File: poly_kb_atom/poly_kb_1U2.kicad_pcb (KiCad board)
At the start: 2 copper layers, 19 x 38.1 mm, 38 parts, among them J1 Conn_01x16, J2 North, J3 WestFront, J4 EastFront, J5 WestBack, J6 EastBack, J7 South, J8 North2, J9 South2, SW1 SW_Push

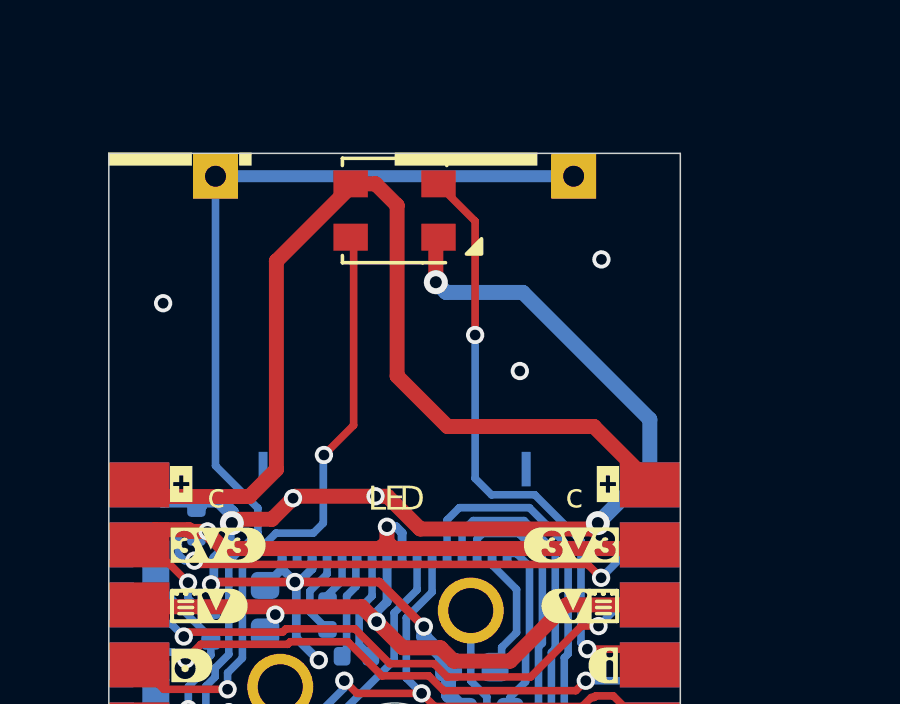
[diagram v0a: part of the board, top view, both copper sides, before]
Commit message: Added optional C7 and fix LED silkscreens
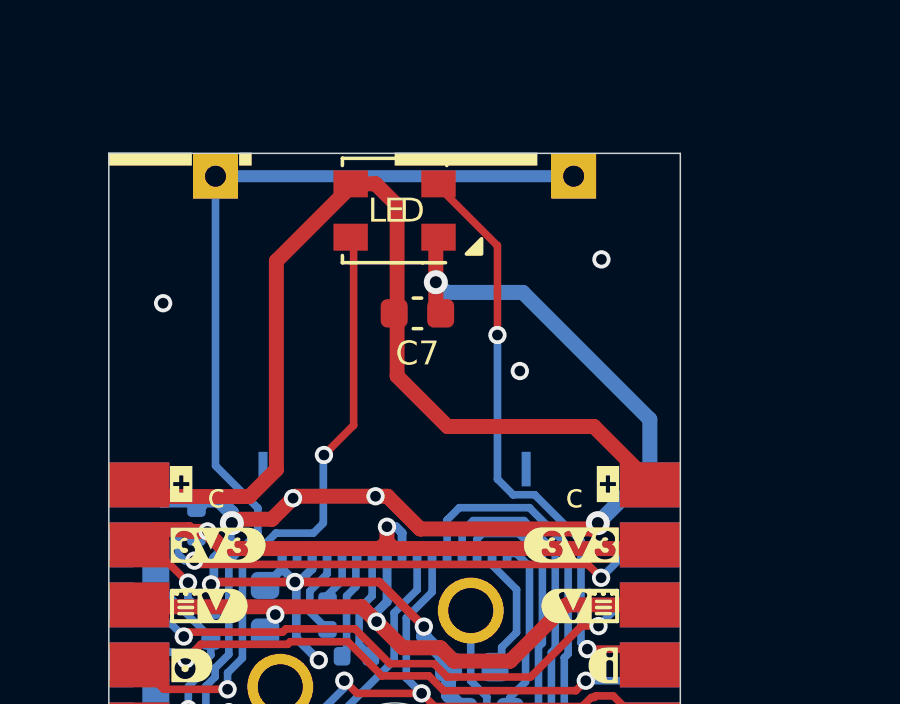
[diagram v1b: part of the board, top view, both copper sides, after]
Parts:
- added C7: 100nF, Capacitor_SMD:C_0603_1608Metric, F.Cu at (102.5, 50.0)
- LED1: value LED -> WS2812B-Mini
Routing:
- net /Keyboard/sheet605ED2EB/GND: track 52.9 -> 54.0 mm
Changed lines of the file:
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@@
       (effects (font (size 0.6 0.6) (thickness 0.15)))
     )
-    (fp_text value "LED" (at 0 0 180) (layer "F.Fab")
+    (fp_text value "WS2812B-Mini" (at 0 0 180) (layer "F.Fab")
       (effects (font (size 0.6 0.6) (thickness 0.15)))
     )
@@
       ) (layer "F.SilkS") (width 0) (fill solid))
   )
+  (footprint "Capacitor_SMD:C_0603_1608Metric" (layer "F.Cu")
+    (at 102.489 49.9618)
+    (descr "Capacitor SMD 0603 (1608 Metric), square (rectangular) end terminal, IPC_7351 nominal, (Body size source: IPC-SM-782 page 76, https://www.pcb-3d.com/wordpress/wp-content/uploads/ipc-sm-782a_amendment_1_and_2.pdf), generated with kicad-footprint-generator")
+    (tags "capacitor")
+    (property "LCSC" "C19666")
+    (property "Sheetfile" "SSD1306_TO_SPI.kicad_sch")
+    (property "Sheetname" "sheet605ED2EB")
+    (attr smd)
+    (fp_text reference "C7" (at 0 1.3335) (layer "F.SilkS")
+      (effects (font (size 0.8 0.8) (thickness 0.15)))
+    )
+    (fp_text value "100nF" (at 0 1.43) (layer "F.Fab")
+      (effects (font (size 1 1) (thickness 0.15)))
+    )
+    (fp_text user "${REFERENCE}" (at 0 0) (layer "F.Fab")
+      (effects (font (size 0.4 0.4) (thickness 0.06)))
+    )
+    (fp_line (start -0.14058 -0.51) (end 0.14058 -0.51) (layer "F.SilkS") (width 0.12))
+    (fp_line (start -0.14058 0.51) (end 0.14058 0.51) (layer "F.SilkS") (width 0.12))
+    (fp_line (start 1.48 -0.73) (end 1.48 0.73) (layer "F.CrtYd") (width 0.05))
+    (fp_line (start 1.48 0.73) (end -1.48 0.73) (layer "F.CrtYd") (width 0.05))
+    (fp_line (start -1.48 0.73) (end -1.48 -0.73) (layer "F.CrtYd") (width 0.05))
+    (fp_line (start -1.48 -0.73) (end 1.48 -0.73) (layer "F.CrtYd") (width 0.05))
+    (fp_line (start 0.8 0.4) (end -0.8 0.4) (layer "F.Fab") (width 0.1))
+    (fp_line (start 0.8 -0.4) (end 0.8 0.4) (layer "F.Fab") (width 0.1))
+    (fp_line (start -0.8 0.4) (end -0.8 -0.4) (layer "F.Fab") (width 0.1))
+    (fp_line (start -0.8 -0.4) (end 0.8 -0.4) (layer "F.Fab") (width 0.1))
+    (pad "1" smd roundrect (at -0.775 0) (size 0.9 0.95) (layers "F.Cu" "F.Paste" "F.Mask") (roundrect_rratio 0.25)
+      (net 15 "/Keyboard/sheet605ED2EB/5V") (pintype "passive"))
+    (pad "2" smd roundrect (at 0.775 0) (size 0.9 0.95) (layers "F.Cu" "F.Paste" "F.Mask") (roundrect_rratio 0.25)
+      (net 1 "/Keyboard/sheet605ED2EB/GND") (pintype "passive"))
+    (model "${KICAD6_3DMODEL_DIR}/Capacitor_SMD.3dshapes/C_0603_1608Metric.wrl"
+      (offset (xyz 0 0 0))
+      (scale (xyz 1 1 1))
+      (rotate (xyz 0 0 0))
+    )
+  )
   (footprint "kibuzzard-61EFBE87" (layer "F.Cu")
     (at 96.0374 59.7154)
@@
     (effects (font (size 0.8 0.8) (thickness 0.153)))
   )
-  (gr_text "E" (at 101.727 56.134) (layer "F.SilkS")
+  (gr_text "E" (at 101.727 46.5328) (layer "F.SilkS")
     (effects (font (size 0.8 0.8) (thickness 0.15)))
   )
-  (gr_text "D" (at 102.3112 56.134) (layer "F.SilkS")
+  (gr_text "D" (at 102.3112 46.5328) (layer "F.SilkS")
     (effects (font (size 0.8 0.8) (thickness 0.15)))
   )
-  (gr_text "L" (at 101.1428 56.134) (layer "F.SilkS")
+  (gr_text "L" (at 101.1428 46.5328) (layer "F.SilkS")
     (effects (font (size 0.8 0.8) (thickness 0.15)))
   )
@@
   (segment (start 101.092 56.0578) (end 98.407521 56.0578) (width 0.5) (layer "F.Cu") (net 1))
   (segment (start 95.662917 58.91646) (end 95.585745 58.993632) (width 0.2921) (layer "F.Cu") (net 1))
+  (segment (start 103.102 48.9228) (end 103.102 49.7998) (width 0.5) (layer "F.Cu") (net 1))
   (segment (start 101.490858 56.0578) (end 102.581996 57.148938) (width 0.5) (layer "F.Cu") (net 1))
   (segment (start 103.102 47.4328) (end 103.092 47.4228) (width 0.5) (layer "F.Cu") (net 1))
@@
   (segment (start 96.503206 56.824825) (end 97.640496 56.824825) (width 0.5) (layer "F.Cu") (net 1))
   (segment (start 103.102 48.9228) (end 103.102 47.4328) (width 0.5) (layer "F.Cu") (net 1))
+  (segment (start 103.102 49.7998) (end 103.264 49.9618) (width 0.5) (layer "F.Cu") (net 1))
   (segment (start 108.305862 57.148938) (end 108.502 56.9528) (width 0.5) (layer "F.Cu") (net 1))
   (via (at 99.202 61.5188) (size 0.6096) (drill 0.3556) (layers "F.Cu" "B.Cu") (net 1))
@@
   (segment (start 105.6641 64.427199) (end 105.6641 65.654078) (width 0.254) (layer "B.Cu") (net 13))
   (segment (start 109.457 61.1528) (end 108.152 61.1528) (width 0.254) (layer "F.Cu") (net 14))
-  (segment (start 104.412 46.8878) (end 104.412 50.6828) (width 0.254) (layer "F.Cu") (net 14))
   (segment (start 94.032638 62.492438) (end 96.160345 62.492438) (width 0.254) (layer "F.Cu") (net 14))
   (segment (start 99.372 54.6828) (end 100.362 53.6928) (width 0.254) (layer "F.Cu") (net 14))
-  (segment (start 103.167 45.6428) (end 104.412 46.8878) (width 0.254) (layer "F.Cu") (net 14))
   (segment (start 100.362 53.6928) (end 100.362 47.4228) (width 0.254) (layer "F.Cu") (net 14))
+  (segment (start 103.092 45.6428) (end 105.156 47.7068) (width 0.254) (layer "F.Cu") (net 14))
   (segment (start 109.982 61.6778) (end 109.457 61.1528) (width 0.254) (layer "F.Cu") (net 14))
   (segment (start 93.218 61.6778) (end 94.032638 62.492438) (width 0.254) (layer "F.Cu") (net 14))
-  (segment (start 103.092 45.6428) (end 103.167 45.6428) (width 0.254) (layer "F.Cu") (net 14))
+  (segment (start 105.156 47.7068) (end 105.156 50.6828) (width 0.254) (layer "F.Cu") (net 14))
   (via (at 108.152 61.1528) (size 0.6096) (drill 0.3556) (layers "F.Cu" "B.Cu") (net 14))
   (via (at 96.160345 62.492438) (size 0.6096) (drill 0.3556) (layers "F.Cu" "B.Cu") (net 14))
-  (via (at 104.412 50.6828) (size 0.6096) (drill 0.3556) (layers "F.Cu" "B.Cu") (net 14))
+  (via (at 105.156 50.6828) (size 0.6096) (drill 0.3556) (layers "F.Cu" "B.Cu") (net 14))
   (via (at 99.372 54.6828) (size 0.6096) (drill 0.3556) (layers "F.Cu" "B.Cu") (net 14))
   (segment (start 96.160345 61.944455) (end 96.160345 62.492438) (width 0.254) (layer "B.Cu") (net 14))
-  (segment (start 106.398853 56.008789) (end 104.957033 56.008789) (width 0.254) (layer "B.Cu") (net 14))
-  (segment (start 107.941555 57.551491) (end 106.398853 56.008789) (width 0.254) (layer "B.Cu") (net 14))
-  (segment (start 104.412 55.463756) (end 104.412 50.6828) (width 0.254) (layer "B.Cu") (net 14))
   (segment (start 96.65448 58.404821) (end 96.65448 61.45032) (width 0.254) (layer "B.Cu") (net 14))
+  (segment (start 107.941555 57.551491) (end 106.398853 56.008789) (width 0.254) (layer "B.Cu") (net 14))
   (segment (start 97.772189 57.287111) (end 96.65448 58.404821) (width 0.254) (layer "B.Cu") (net 14))
-  (segment (start 107.941555 60.942355) (end 107.941555 57.551491) (width 0.254) (layer "B.Cu") (net 14))
   (segment (start 99.352 56.9528) (end 99.352 54.7028) (width 0.254) (layer "B.Cu") (net 14))
-  (segment (start 108.152 61.1528) (end 107.941555 60.942355) (width 0.254) (layer "B.Cu") (net 14))
-  (segment (start 104.957033 56.008789) (end 104.412 55.463756) (width 0.254) (layer "B.Cu") (net 14))
   (segment (start 99.017689 57.287111) (end 97.772189 57.287111) (width 0.254) (layer "B.Cu") (net 14))
   (segment (start 99.352 54.7028) (end 99.372 54.6828) (width 0.254) (layer "B.Cu") (net 14))
+  (segment (start 108.152 61.1528) (end 107.941555 60.942355) (width 0.254) (layer "B.Cu") (net 14))
+  (segment (start 107.941555 60.942355) (end 107.941555 57.551491) (width 0.254) (layer "B.Cu") (net 14))
+  (segment (start 106.398853 56.008789) (end 105.678489 56.008789) (width 0.254) (layer "B.Cu") (net 14))
+  (segment (start 105.678489 56.008789) (end 105.156 55.4863) (width 0.254) (layer "B.Cu") (net 14))
+  (segment (start 105.156 55.4863) (end 105.156 50.6828) (width 0.254) (layer "B.Cu") (net 14))
   (segment (start 96.65448 61.45032) (end 96.160345 61.944455) (width 0.254) (layer "B.Cu") (net 14))
   (segment (start 99.352 56.9528) (end 99.017689 57.287111) (width 0.254) (layer "B.Cu") (net 14))
